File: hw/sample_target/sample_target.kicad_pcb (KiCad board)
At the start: 2 copper layers, 39.7 x 14 mm, 28 parts, among them J1 USB_C_Receptacle, SW1 BTN, SW2 BTN, U1 SN74AHC1G08DBVRG4, U2 MIC5504-3.3YM5, U3 TMUX1511PWR, U4 STM32L412C8T6

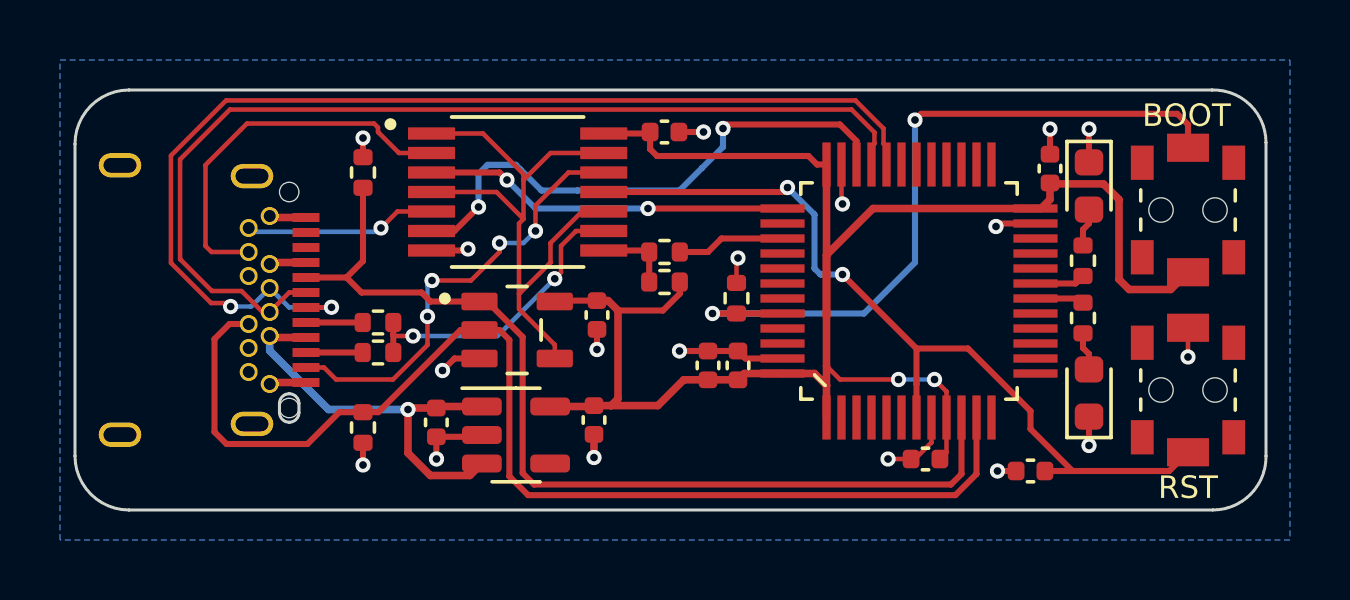
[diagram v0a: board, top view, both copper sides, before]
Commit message: Added opamp to sample target
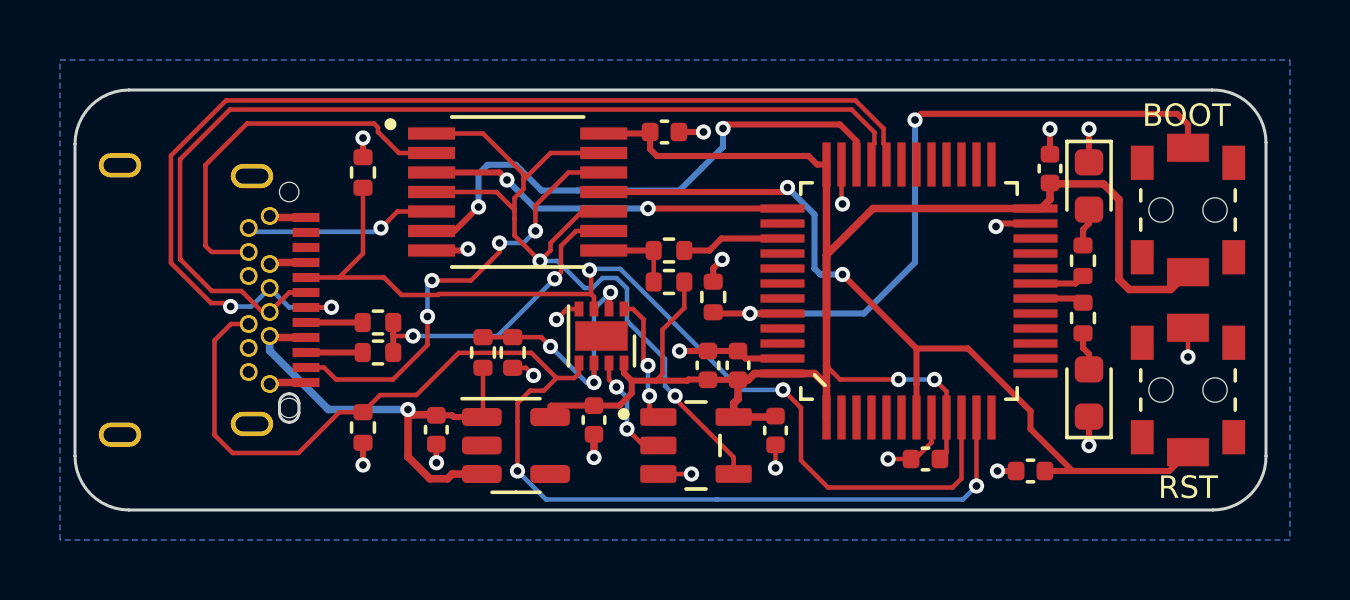
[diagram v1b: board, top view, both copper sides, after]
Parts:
- added R10: 240k, Resistor_SMD:R_0402_1005Metric, F.Cu at (125.1, 131.8)
- added R11: 10k, Resistor_SMD:R_0402_1005Metric, F.Cu at (126.1, 131.8)
- added U5: LM358_DFN, Package_DFN_QFN:DFN-8-1EP_2x2mm_P0.5mm_EP1.05x1.75mm, F.Cu at (129.1, 131.2)
- moved U1 7.10 mm to (132.2, 134.8)
- moved C3 7.09 mm to (134.8, 134.3)
- moved R9 0.78 mm to (132.8, 129.9)
- moved U2 0.35 mm to (126.2, 134.8)
- moved C1 0.24 mm to (123.5, 134.3)
- moved R6 0.16 mm to (131.3, 128.3)
- moved R5 0.15 mm to (131.3, 129.4)
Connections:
- U1 pad 1: /CC1 -> /CC1_AMP
- U1 pad 2: /CC2 -> /CC2_AMP
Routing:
- net /VREF: track 0.00 -> 8.77 mm, vias 0 -> 3
- net /DAM_EN: track 21.2 -> 27.3 mm, vias 0 -> 2
- net /CC1_AMP: track 0.00 -> 4.25 mm, vias 0 -> 2
- net /CC2_AMP: track 0.00 -> 3.72 mm, vias 0 -> 2
- net /CC2: track 38.7 -> 41.1 mm, vias 0 -> 2
- net VBUS: track 15.3 -> 17.3 mm
- net /BOOT: track 24.6 -> 23.4 mm
- net VCC: track 60.1 -> 59.2 mm
- net /CC1: track 32.6 -> 33.1 mm, vias 0 -> 2
- net GND: track 25.1 -> 25.0 mm, vias 18 -> 20
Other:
- board text added: "v1.1 by @alvaroprieto"
- board text removed: "v1.0 by @alvaroprieto"
